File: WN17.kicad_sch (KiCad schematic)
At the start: 4 parts, among them J1 Conn_01x02_Pin, U1 AS5600, U2 DRV8434APWPR

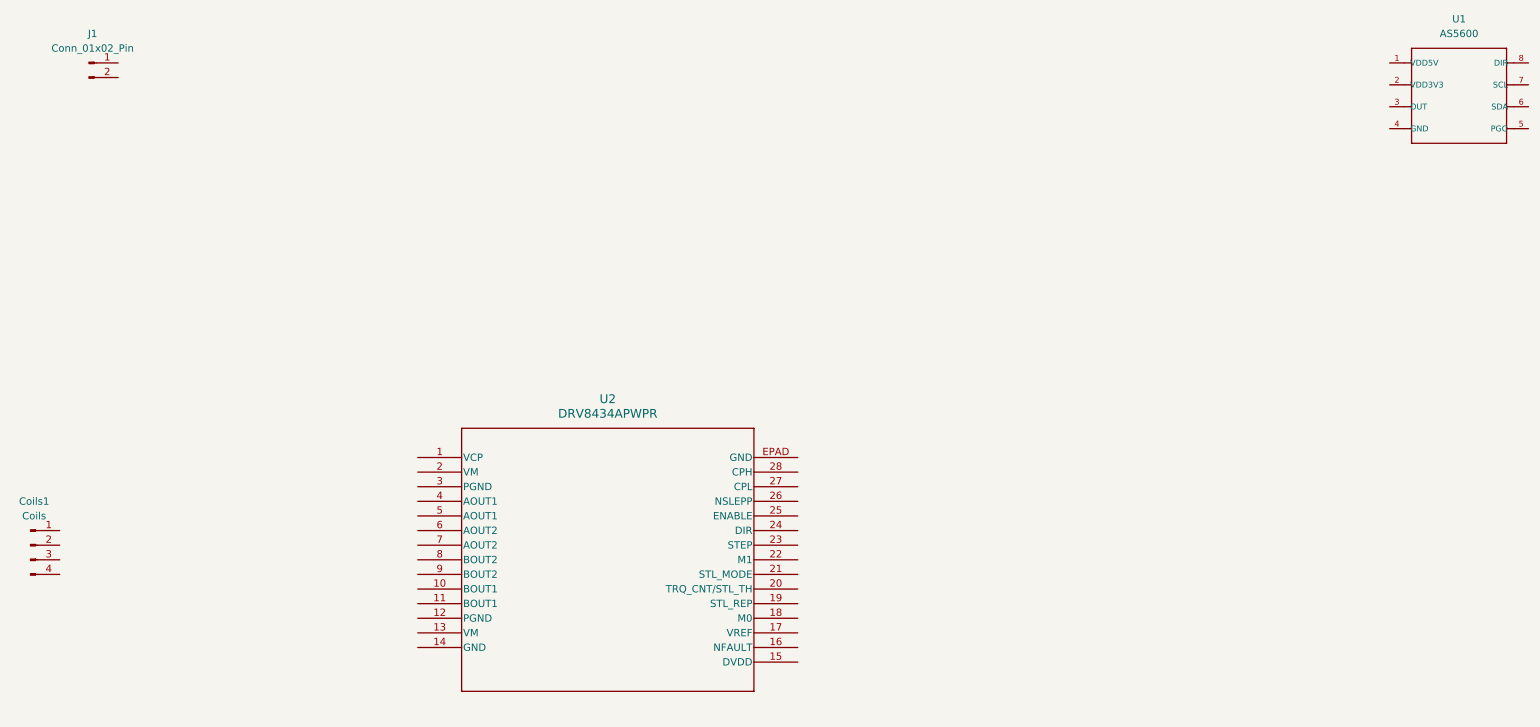
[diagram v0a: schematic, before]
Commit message: Added Motor driver capacitors and  supply
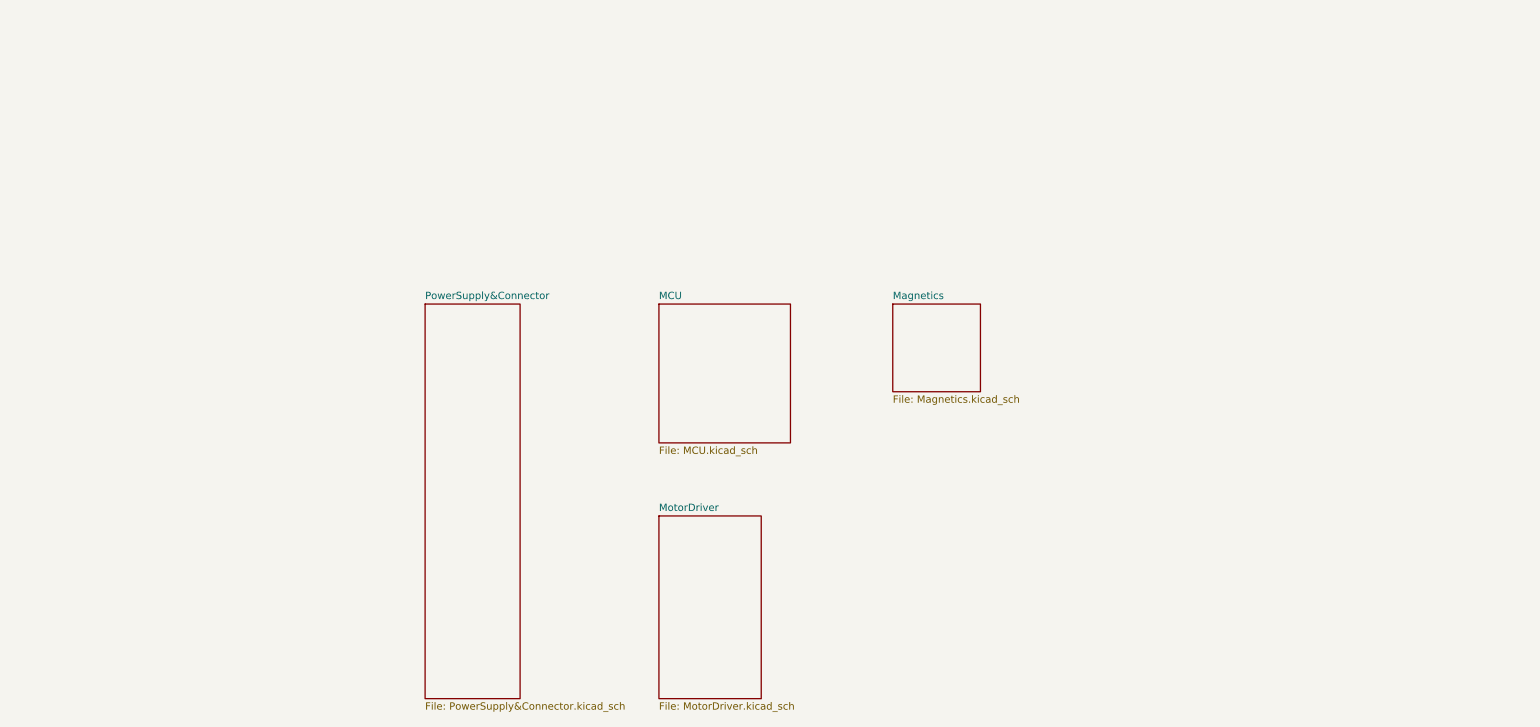
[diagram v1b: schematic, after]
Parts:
- removed Coils1: Coils, Connector_PinHeader_2.54mm:PinHeader_1x04_P2.54mm_Vertical, symbol Connector:Conn_01x04_Pin
- removed J1: Conn_01x02_Pin, Connector_PinHeader_2.54mm:PinHeader_1x02_P2.54mm_Vertical, symbol Connector:Conn_01x02_Pin
- removed U1: AS5600, libraries:AS5600, symbol AS5600:AS5600
- removed U2: DRV8434APWPR, DRV8434APWPR_TEX, symbol drv8411:DRV8434APWPR
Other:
- added sheet MCU (MCU.kicad_sch)
- added sheet Magnetics (Magnetics.kicad_sch)
- added sheet MotorDriver (MotorDriver.kicad_sch)
- added sheet PowerSupply&Connector (PowerSupply&Connector.kicad_sch)

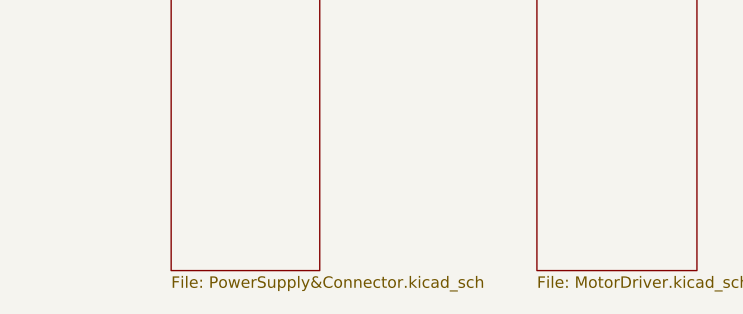
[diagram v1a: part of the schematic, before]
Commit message: Etiquetas y pines modulo driver
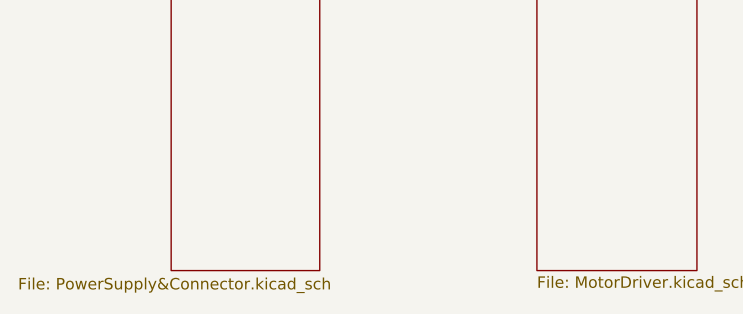
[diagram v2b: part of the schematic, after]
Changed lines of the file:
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@@
 		(at 87.63 67.31)
 		(size 16.51 68.58)
-		(fields_autoplaced yes)
 		(stroke
 			(width 0.1524)
@@
 		)
 		(property "Sheetfile" "PowerSupply&Connector.kicad_sch"
-			(at 87.63 136.4746 0)
+			(at 70.612 136.652 0)
 			(effects
 				(font

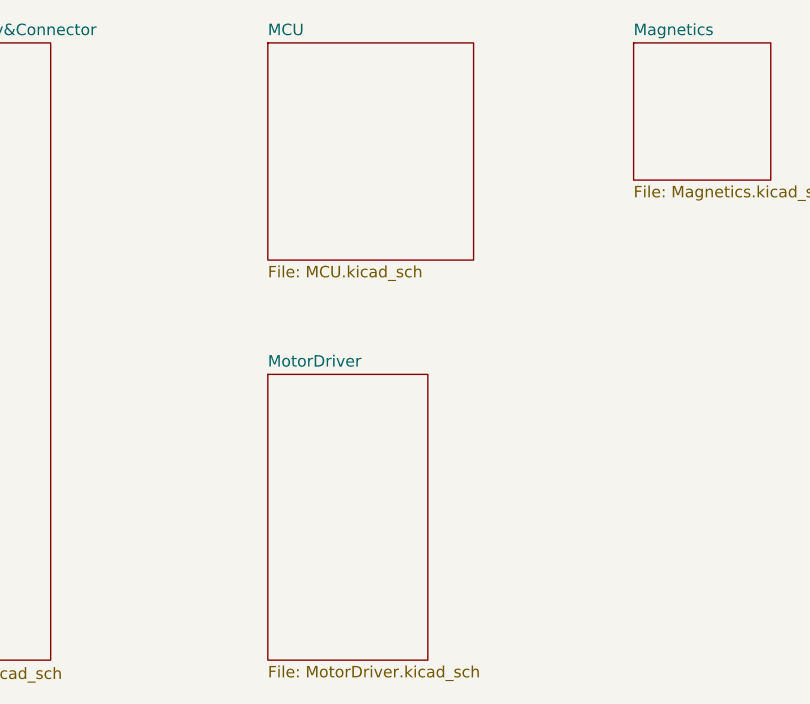
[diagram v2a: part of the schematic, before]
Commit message: Finished motor driver
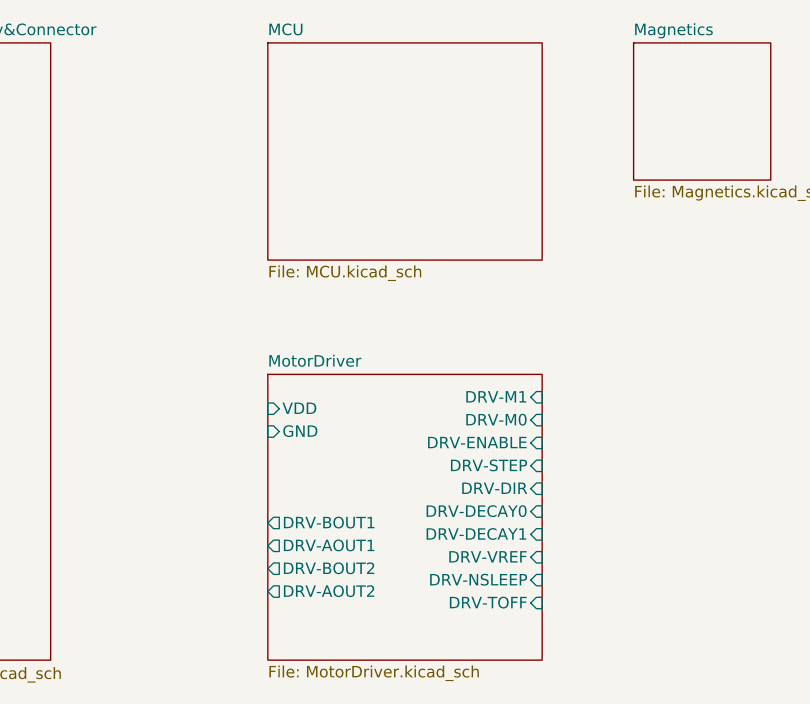
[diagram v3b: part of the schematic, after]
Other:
- sheet MotorDriver ports: added DRV-AOUT1, DRV-AOUT2, DRV-BOUT1, DRV-BOUT2, DRV-DECAY0, DRV-DECAY1, DRV-DIR, DRV-ENABLE, DRV-M0, DRV-M1, DRV-NSLEEP, DRV-STEP, DRV-TOFF, DRV-VREF, GND, VDD; removed none
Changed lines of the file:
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@@
 	(sheet
 		(at 128.27 104.14)
-		(size 17.78 31.75)
+		(size 30.48 31.75)
 		(fields_autoplaced yes)
 		(stroke
@@
 				)
 				(justify left top)
+			)
+		)
+		(pin "VDD" input
+			(at 128.27 107.95 180)
+			(effects
+				(font
+					(size 1.27 1.27)
+				)
+				(justify left)
+			)
+		)
+		(pin "DRV-BOUT1" output
+			(at 128.27 120.65 180)
+			(effects
+				(font
+					(size 1.27 1.27)
+				)
+				(justify left)
+			)
+		)
+		(pin "DRV-AOUT1" output
+			(at 128.27 123.19 180)
+			(effects
+				(font
+					(size 1.27 1.27)
+				)
+				(justify left)
+			)
+		)
+		(pin "DRV-BOUT2" output
+			(at 128.27 125.73 180)
+			(effects
+				(font
+					(size 1.27 1.27)
+				)
+				(justify left)
+			)
+		)
+		(pin "DRV-AOUT2" output
+			(at 128.27 128.27 180)
+			(effects
+				(font
+					(size 1.27 1.27)
+				)
+				(justify left)
+			)
+		)
+		(pin "GND" input
+			(at 128.27 110.49 180)
+			(effects
+				(font
+					(size 1.27 1.27)
+				)
+				(justify left)
+			)
+		)
+		(pin "DRV-M1" input
+			(at 158.75 106.68 0)
+			(effects
+				(font
+					(size 1.27 1.27)
+				)
+				(justify right)
+			)
+		)
+		(pin "DRV-DIR" input
+			(at 158.75 116.84 0)
+			(effects
+				(font
+					(size 1.27 1.27)
+				)
+				(justify right)
+			)
+		)
+		(pin "DRV-ENABLE" input
+			(at 158.75 111.76 0)
+			(effects
+				(font
+					(size 1.27 1.27)
+				)
+				(justify right)
+			)
+		)
+		(pin "DRV-STEP" input
+			(at 158.75 114.3 0)
+			(effects
+				(font
+					(size 1.27 1.27)
+				)
+				(justify right)
+			)
+		)
+		(pin "DRV-NSLEEP" input
+			(at 158.75 127 0)
+			(effects
+				(font
+					(size 1.27 1.27)
+				)
+				(justify right)
+			)
+		)
+		(pin "DRV-DECAY0" input
+			(at 158.75 119.38 0)
+			(effects
+				(font
+					(size 1.27 1.27)
+				)
+				(justify right)
+			)
+		)
+		(pin "DRV-DECAY1" input
+			(at 158.75 121.92 0)
+			(effects
+				(font
+					(size 1.27 1.27)
+				)
+				(justify right)
+			)
+		)
+		(pin "DRV-VREF" input
+			(at 158.75 124.46 0)
+			(effects
+				(font
+					(size 1.27 1.27)
+				)
+				(justify right)
+			)
+		)
+		(pin "DRV-M0" input
+			(at 158.75 109.22 0)
+			(effects
+				(font
+					(size 1.27 1.27)
+				)
+				(justify right)
+			)
+		)
+		(pin "DRV-TOFF" input
+			(at 158.75 129.54 0)
+			(effects
+				(font
+					(size 1.27 1.27)
+				)
+				(justify right)
 			)
 		)
@@
 	(sheet
 		(at 128.27 67.31)
-		(size 22.86 24.13)
+		(size 30.48 24.13)
 		(fields_autoplaced yes)
 		(stroke

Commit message: Ordered coils
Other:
- sheet PowerSupply&Connector ports: added +3.3V, GND, VDD, coil-A+, coil-A-, coil-B+, coil-B-; removed none
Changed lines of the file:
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@@
 	(generator_version "8.0")
 	(paper "A4")
+	(wire
+		(pts
+			(xy 104.14 107.95) (xy 128.27 107.95)
+		)
+		(stroke
+			(width 0)
+			(type default)
+		)
+	)
+	(wire
+		(pts
+			(xy 104.14 121.92) (xy 128.27 121.92)
+		)
+		(stroke
+			(width 0)
+			(type default)
+		)
+	)
+	(wire
+		(pts
+			(xy 104.14 110.49) (xy 128.27 110.49)
+		)
+		(stroke
+			(width 0)
+			(type default)
+		)
+	)
+	(wire
+		(pts
+			(xy 104.14 119.38) (xy 128.27 119.38)
+		)
+		(stroke
+			(width 0)
+			(type default)
+		)
+	)
+	(wire
+		(pts
+			(xy 104.14 127) (xy 128.27 127)
+		)
+		(stroke
+			(width 0)
+			(type default)
+		)
+	)
+	(wire
+		(pts
+			(xy 104.14 124.46) (xy 128.27 124.46)
+		)
+		(stroke
+			(width 0)
+			(type default)
+		)
+	)
 	(sheet
 		(at 128.27 104.14)
@@
 		)
 		(pin "DRV-BOUT1" output
-			(at 128.27 120.65 180)
+			(at 128.27 124.46 180)
 			(effects
 				(font
@@
 		)
 		(pin "DRV-AOUT1" output
-			(at 128.27 123.19 180)
+			(at 128.27 119.38 180)
 			(effects
 				(font
@@
 		)
 		(pin "DRV-BOUT2" output
-			(at 128.27 125.73 180)
+			(at 128.27 127 180)
 			(effects
 				(font
@@
 		)
 		(pin "DRV-AOUT2" output
-			(at 128.27 128.27 180)
+			(at 128.27 121.92 180)
 			(effects
 				(font
@@
 			)
 		)
+		(pin "+3.3V" output
+			(at 104.14 71.12 0)
+			(effects
+				(font
+					(size 1.27 1.27)
+				)
+				(justify right)
+			)
+		)
+		(pin "coil-A-" input
+			(at 104.14 119.38 0)
+			(effects
+				(font
+					(size 1.27 1.27)
+				)
+				(justify right)
+			)
+		)
+		(pin "coil-A+" input
+			(at 104.14 121.92 0)
+			(effects
+				(font
+					(size 1.27 1.27)
+				)
+				(justify right)
+			)
+		)
+		(pin "coil-B+" input
+			(at 104.14 124.46 0)
+			(effects
+				(font
+					(size 1.27 1.27)
+				)
+				(justify right)
+			)
+		)
+		(pin "coil-B-" input
+			(at 104.14 127 0)
+			(effects
+				(font
+					(size 1.27 1.27)
+				)
+				(justify right)
+			)
+		)
+		(pin "GND" output
+			(at 104.14 110.49 0)
+			(effects
+				(font
+					(size 1.27 1.27)
+				)
+				(justify right)
+			)
+		)
+		(pin "VDD" output
+			(at 104.14 107.95 0)
+			(effects
+				(font
+					(size 1.27 1.27)
+				)
+				(justify right)
+			)
+		)

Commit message: Updates
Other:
- sheet MCU ports: added +3.3V, GND; removed none
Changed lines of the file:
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@@
 	(generator_version "8.0")
 	(paper "A4")
+	(junction
+		(at 115.57 110.49)
+		(diameter 0)
+		(color 0 0 0 0)
+	)
 	(wire
 		(pts
@@
 	(wire
 		(pts
+			(xy 115.57 110.49) (xy 128.27 110.49)
+		)
+		(stroke
+			(width 0)
+			(type default)
+		)
+	)
+	(wire
+		(pts
 			(xy 104.14 121.92) (xy 128.27 121.92)
 		)
@@
 	(wire
 		(pts
-			(xy 104.14 110.49) (xy 128.27 110.49)
+			(xy 104.14 110.49) (xy 115.57 110.49)
+		)
+		(stroke
+			(width 0)
+			(type default)
+		)
+	)
+	(wire
+		(pts
+			(xy 104.14 71.12) (xy 128.27 71.12)
 		)
 		(stroke
@@
 		(pts
 			(xy 104.14 127) (xy 128.27 127)
+		)
+		(stroke
+			(width 0)
+			(type default)
+		)
+	)
+	(wire
+		(pts
+			(xy 128.27 73.66) (xy 115.57 73.66)
+		)
+		(stroke
+			(width 0)
+			(type default)
+		)
+	)
+	(wire
+		(pts
+			(xy 115.57 73.66) (xy 115.57 110.49)
 		)
 		(stroke
@@
 	)
 	(sheet
-		(at 168.91 67.31)
+		(at 201.93 67.31)
 		(size 15.24 15.24)
 		(fields_autoplaced yes)
@@
 		)
 		(property "Sheetname" "Magnetics"
-			(at 168.91 66.5984 0)
+			(at 201.93 66.5984 0)
 			(effects
 				(font
@@
 		)
 		(property "Sheetfile" "Magnetics.kicad_sch"
-			(at 168.91 83.1346 0)
+			(at 201.93 83.1346 0)
 			(effects
 				(font
@@
 			)
 		)
+		(pin "+3.3V" input
+			(at 128.27 71.12 180)
+			(effects
+				(font
+					(size 1.27 1.27)
+				)
+				(justify left)
+			)
+		)
+		(pin "GND" input
+			(at 128.27 73.66 180)
+			(effects
+				(font
+					(size 1.27 1.27)
+				)
+				(justify left)
+			)
+		)

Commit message: uPDATE
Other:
- sheet PowerSupply&Connector ports: added MCP6C02_VOUT; removed none
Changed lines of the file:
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@@
 	(wire
 		(pts
-			(xy 128.27 73.66) (xy 115.57 73.66)
+			(xy 128.27 77.47) (xy 115.57 77.47)
 		)
 		(stroke
@@
 	(wire
 		(pts
-			(xy 115.57 73.66) (xy 115.57 110.49)
+			(xy 115.57 77.47) (xy 115.57 110.49)
 		)
 		(stroke
@@
 			)
 		)
+		(pin "MCP6C02_VOUT" output
+			(at 104.14 74.93 0)
+			(effects
+				(font
+					(size 1.27 1.27)
+				)
+				(justify right)
+			)
+		)
 		(instances
 			(project "WN17"
@@
 		)
 		(pin "GND" input
-			(at 128.27 73.66 180)
-			(effects
-				(font
+			(at 128.27 77.47 180)
+			(effects
+				(font

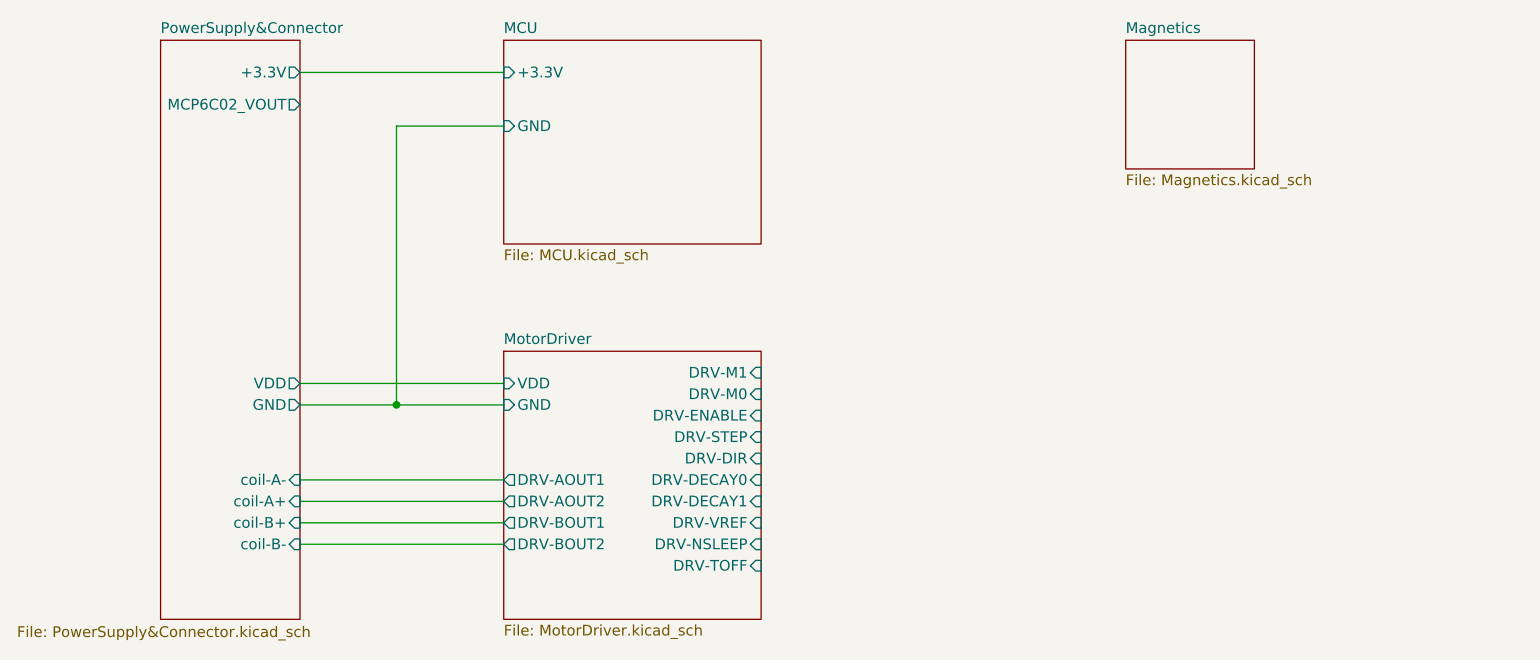
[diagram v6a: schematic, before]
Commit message: Schematic done
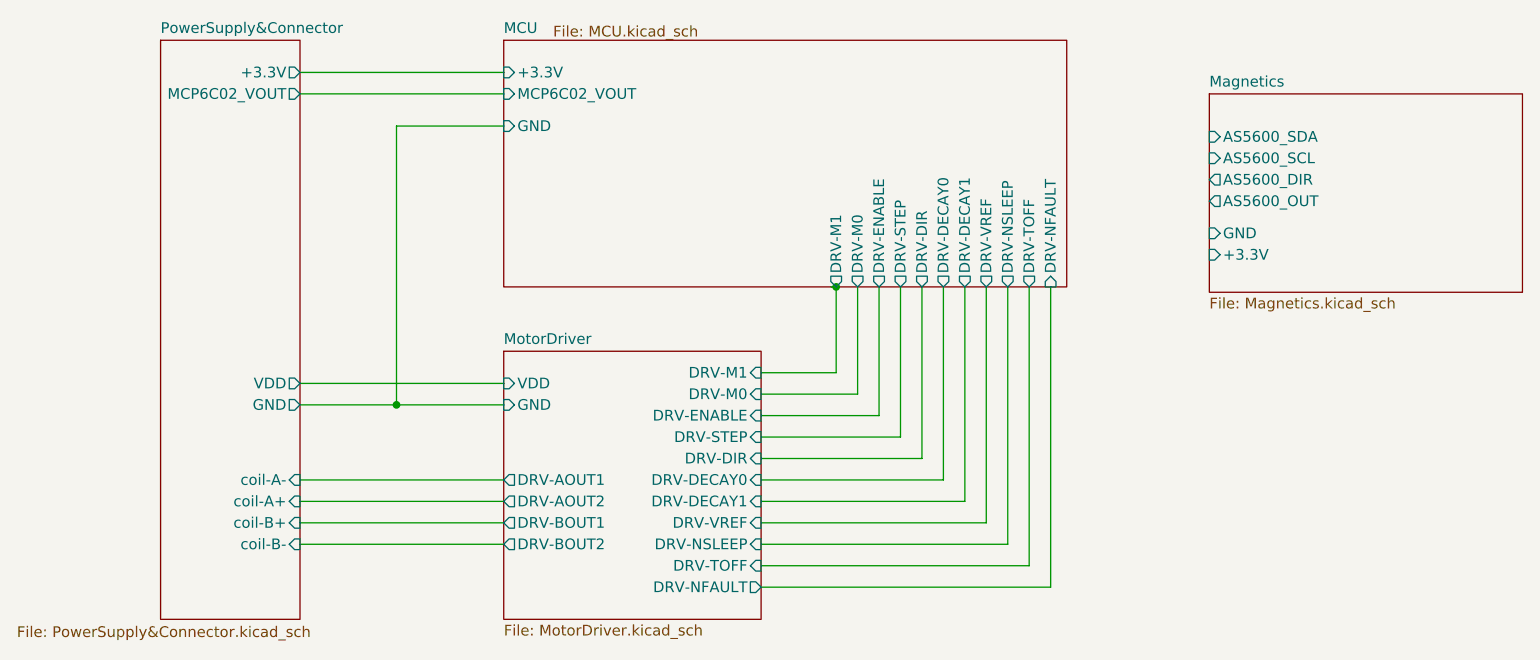
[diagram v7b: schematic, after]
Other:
- sheet MCU ports: added DRV-DECAY0, DRV-DECAY1, DRV-DIR, DRV-ENABLE, DRV-M0, DRV-M1, DRV-NFAULT, DRV-NSLEEP, DRV-STEP, DRV-TOFF, DRV-VREF, MCP6C02_VOUT; removed none
- sheet Magnetics ports: added +3.3V, AS5600_DIR, AS5600_OUT, AS5600_SCL, AS5600_SDA, GND; removed none
- sheet MotorDriver ports: added DRV-NFAULT; removed none
